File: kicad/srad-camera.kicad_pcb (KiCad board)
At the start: 4 copper layers, 50 x 50 mm, 247 parts, among them J1 DEBUG, SW1 PWR, SW2 USER, SW3 BOOT0, U1 AP61300Z6, U2 AP61300Z6, U3 RK809-5, U4 STM32U575RGT6, U5 RK3566, U6 MT41K256M16TW-107:P

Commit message: Minor layout tweaks
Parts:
- C123, C133, C135, C138, C140, C143, C144, C145, C146: moved to F.Cu
- C136, C137: moved to B.Cu
- moved C140 10.2 mm to (59.4, 81.2), turned to 90 degrees
- moved C129 8.54 mm to (69.0, 70.0), turned to 0 degrees
- moved C142 8.35 mm to (69.0, 71.3), turned to 0 degrees
- moved C134 8.33 mm to (60.5, 81.2), turned to 90 degrees
- moved C132 8.11 mm to (60.6, 78.5), turned to -90 degrees
- moved C123 7.93 mm to (67.5, 81.2), turned to 180 degrees
- moved C143 7.88 mm to (60.6, 81.2)
- moved C135 7.04 mm to (67.5, 78.5)
- moved C127 6.62 mm to (69.0, 72.5), turned to 0 degrees
- moved C130 6.38 mm to (59.4, 78.5), turned to -90 degrees
- moved C128 6.05 mm to (69.0, 73.7), turned to 0 degrees
- moved C136 5.61 mm to (67.1, 81.2), turned to 180 degrees
- moved C131 5.05 mm to (61.8, 78.5), turned to -90 degrees
- moved C141 4.86 mm to (63.0, 78.5), turned to -90 degrees
- moved C139 4.13 mm to (64.3, 81.2), turned to 90 degrees
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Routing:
- net GND: track 326.9 -> 350.2 mm, vias 260 -> 255
- net VCC_DDR: track 175.3 -> 169.7 mm, vias 40 -> 48
- net /Power Supply/VIN_5V: track 47.0 -> 50.8 mm, vias 6 -> 3
- net /LSM6DSRTR/SCL: track 19.0 -> 15.5 mm
- net VCCIO_3V3_IMU: track 76.9 -> 73.9 mm
- net /LSM6DSRTR/INT2: track 11.8 -> 8.95 mm
- net MIPI_AVDD_1V8: track 76.6 -> 73.8 mm
- net /LSM6DSRTR/SDA: track 17.2 -> 14.9 mm
- net /RK3566 SoC/VDD_LOGIC: track 45.8 -> 47.9 mm
- net /LSM6DSRTR/INT1: track 17.7 -> 16.1 mm
- net Net-(R12-Pad2): track 3.74 -> 2.29 mm
- net /RK3566 SoC/VCCA_1V8_IMG: track 14.3 -> 15.5 mm
- net /STM32U575RGT6/USART2_RX: track 54.7 -> 53.5 mm
- net /RK3566 SoC/VDDA_0V9: track 51.9 -> 52.7 mm
- net /STM32U575RGT6/USART2_TX: track 55.7 -> 55.0 mm
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
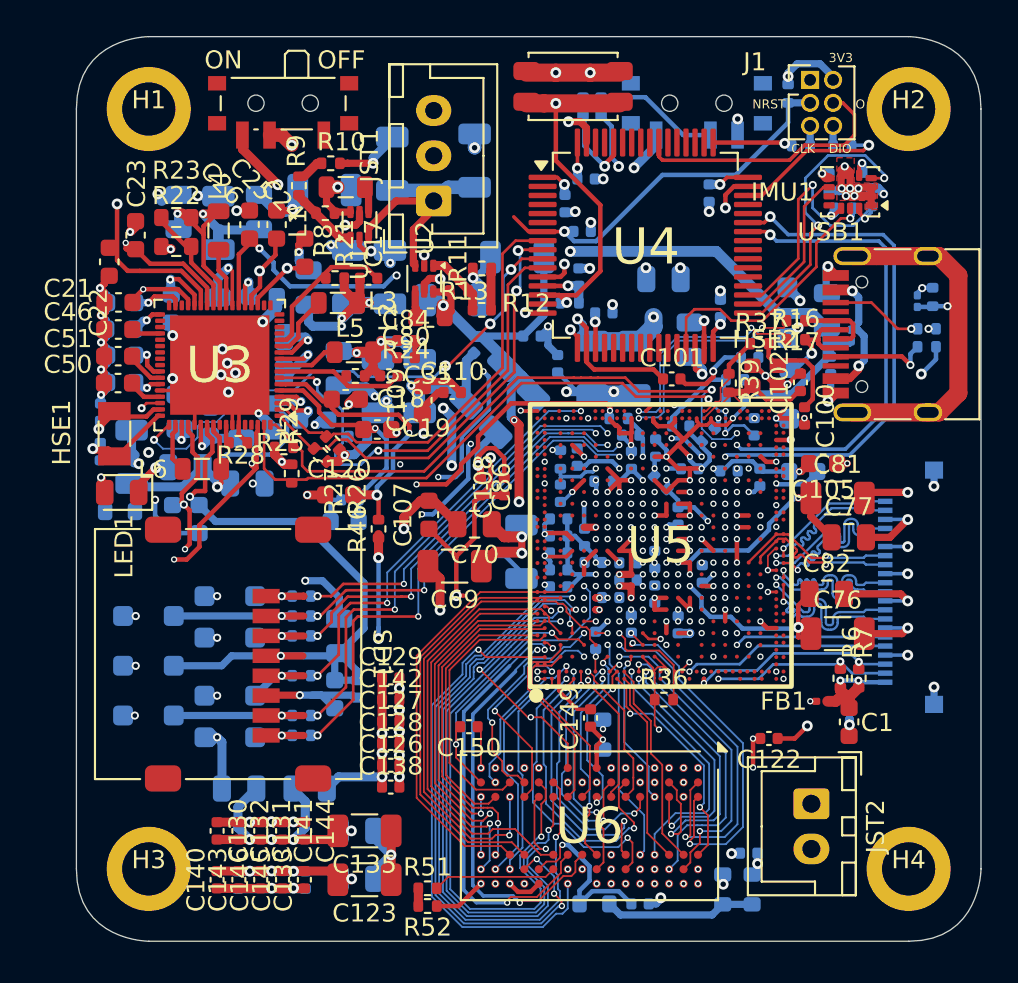
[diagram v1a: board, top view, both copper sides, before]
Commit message: More minor layout tweaks
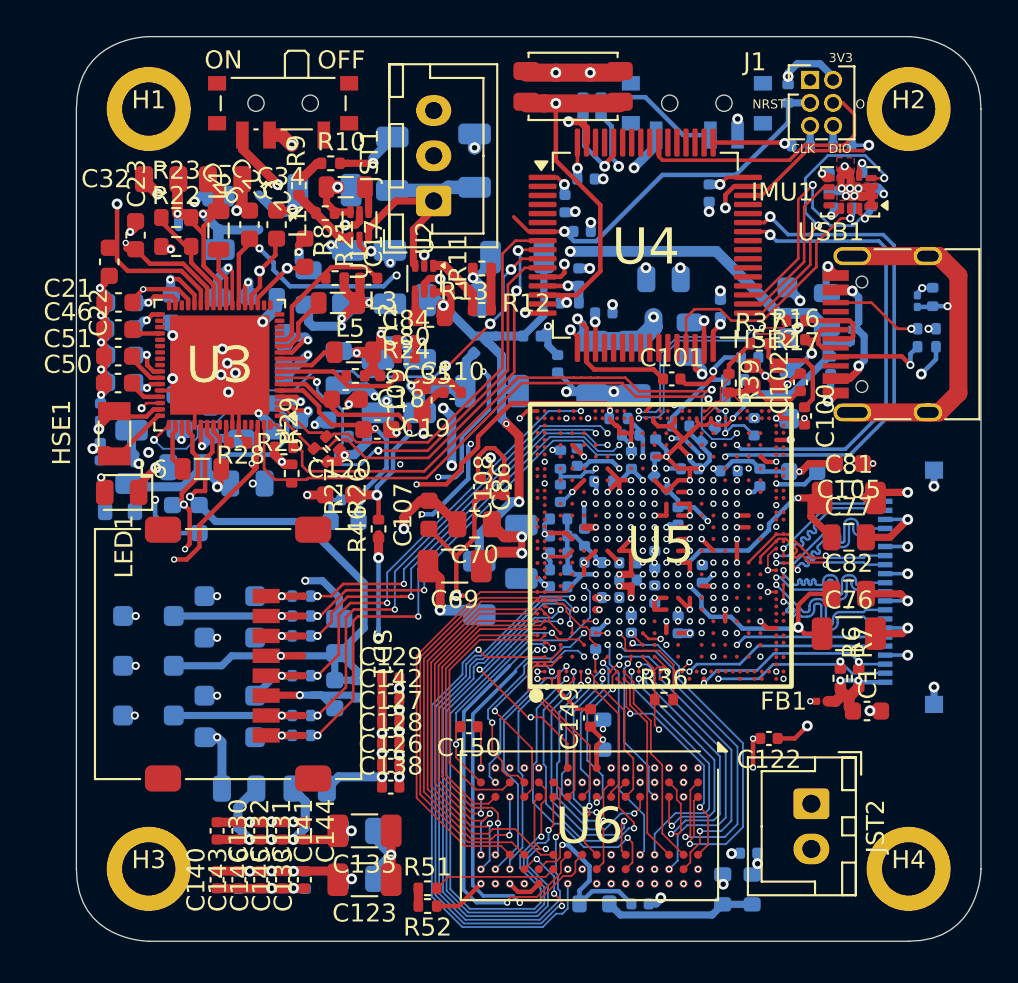
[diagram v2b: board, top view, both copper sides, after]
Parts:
- C32, C34: moved to F.Cu
- moved C65 9.84 mm to (73.9, 65.1), turned to -90 degrees
- moved C34 2.61 mm to (59.8, 42.5), turned to 0 degrees
- moved C32 2.05 mm to (56.3, 42.5), turned to 180 degrees
- moved C105 1.42 mm to (94.3, 58.2)
- moved C82 1.22 mm to (94.3, 65.4)
- moved C1 1.15 mm to (95.3, 71.9), turned to 180 degrees
- moved C76 0.62 mm to (94.3, 67.6)
- moved C81 0.62 mm to (94.3, 60.1)
- moved C64 0.54 mm to (74.6, 54.2), turned to 180 degrees
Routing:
- net /RK3566 SoC/VDD_GPU_NPU: track 76.6 -> 81.5 mm
- net VCC_DDR: track 169.7 -> 173.6 mm
- net VCC_0V9_CPU: track 39.5 -> 42.3 mm
- net /RK3566 SoC/VDDA_0V9_PMU: track 40.0 -> 41.4 mm
- net GND: track 350.2 -> 349.9 mm, vias 255 -> 254

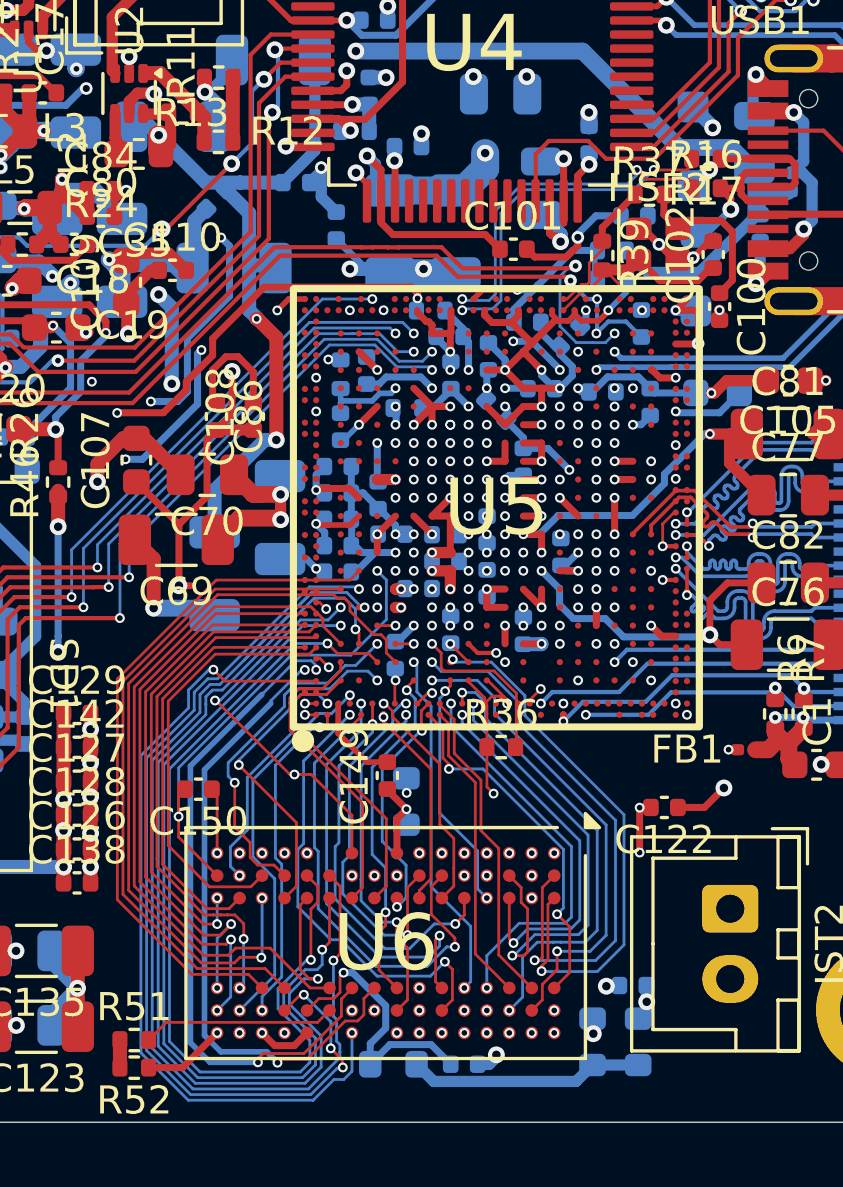
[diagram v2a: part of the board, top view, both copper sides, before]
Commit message: Length matching for DDL3 LDQS
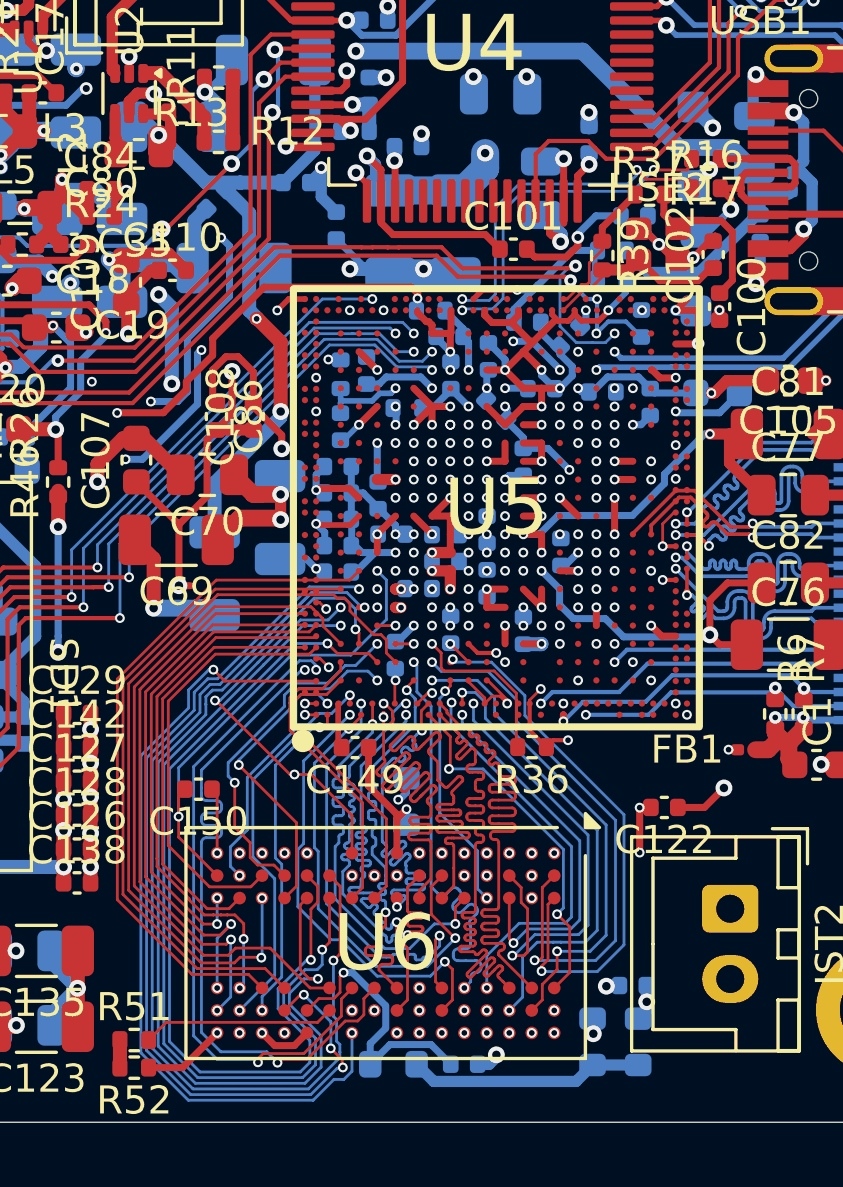
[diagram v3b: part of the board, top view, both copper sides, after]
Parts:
- moved C149 1.52 mm to (78.9, 71.3), turned to 180 degrees
- moved R36 1.10 mm to (85.2, 71.2), turned to 180 degrees
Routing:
- net /MT41K256 DDR3L/DQS_P1: track 10.8 -> 22.7 mm
- net /MT41K256 DDR3L/DQS_N0: track 7.40 -> 19.0 mm
- net /MT41K256 DDR3L/DQS_N1: track 11.5 -> 22.7 mm
- net /MT41K256 DDR3L/DQS_P0: track 8.27 -> 18.9 mm
- net /MT41K256 DDR3L/DQ4: track 8.77 -> 15.7 mm
- net /MT41K256 DDR3L/DQ5: track 12.4 -> 17.1 mm
- net /MT41K256 DDR3L/DQ6: track 13.0 -> 17.2 mm
- net /MT41K256 DDR3L/DM_A0: track 12.5 -> 15.9 mm
- net /MT41K256 DDR3L/DQ7: track 12.4 -> 15.6 mm
- net /MT41K256 DDR3L/CK_P: track 22.5 -> 24.8 mm
- net Net-(U6-V_{REFDQ}): track 3.26 -> 5.21 mm
- net /MT41K256 DDR3L/DQ0: track 14.0 -> 15.6 mm
- net /RK3566 SoC/PMUIO 1-2, OSC/XIN: track 8.70 -> 7.65 mm
- net /MT41K256 DDR3L/VREF_DDR: track 9.18 -> 9.96 mm
- net /MT41K256 DDR3L/DQ1: track 15.0 -> 15.6 mm
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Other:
- board text added: "ADDR, CONTROL, ETC ±1000mil TO CK"
- board text added: "CK ±5mil"
- board text added: "DQ[0..7] ±25mil LDM (DM_A0) ±25mil TO LDQS (750mil)"
- board text added: "DQ[8..15] ±25mil UDM (DM_A1) ±25mil TO UDQS (900mil)"
- board text added: "LDQS ±5mil ±500mil TO UDQS"
- board text added: "UDQS ±5mil"
- board text added: "USB_DN/P 90Ω 10% Z_{D} 5-10mil spacing ±5mil length"

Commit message: Fix length matching for MIPI
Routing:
- net /MT41K256 DDR3L/DM_A1: track 8.60 -> 19.4 mm
- net /MT41K256 DDR3L/DQ8: track 14.2 -> 21.2 mm
- net /MT41K256 DDR3L/DQ12: track 13.0 -> 19.6 mm
- net /MT41K256 DDR3L/DQ9: track 13.4 -> 19.7 mm
- net /MT41K256 DDR3L/DQ11: track 16.3 -> 19.6 mm
- net /MT41K256 DDR3L/DQ10: track 16.3 -> 19.4 mm
- net /MT41K256 DDR3L/DQ14: track 17.0 -> 19.7 mm
- net /RK3566 SoC/MIPI_D0_N: track 7.08 -> 8.80 mm
- net GND: track 349.7 -> 351.3 mm, vias 255 -> 254
- net /RK3566 SoC/MIPI_D1_P: track 10.2 -> 8.66 mm
- net /RK3566 SoC/MIPI_D3_P: track 10.2 -> 8.69 mm
- net /RK3566 SoC/MIPI_D2_N: track 10.2 -> 8.68 mm
- net /RK3566 SoC/MIPI_CN: track 8.76 -> 8.79 mm, vias 1 -> 2
- net /RK3566 SoC/MIPI_CP: track 8.74 -> 8.73 mm, vias 1 -> 2
